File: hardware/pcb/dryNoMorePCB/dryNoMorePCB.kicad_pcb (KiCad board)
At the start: 2 copper layers, 76.2 x 48.6 mm, 47 parts, among them J10 Barrel_Jack_MountingPin, J11 Conn_01x03, J12 Conn_01x03, J13 Conn_01x02, J14 ETH_W5500, J15 Conn_01x02, J16 Conn_01x02, J17 Conn_01x02, J18 GND, J19 GND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

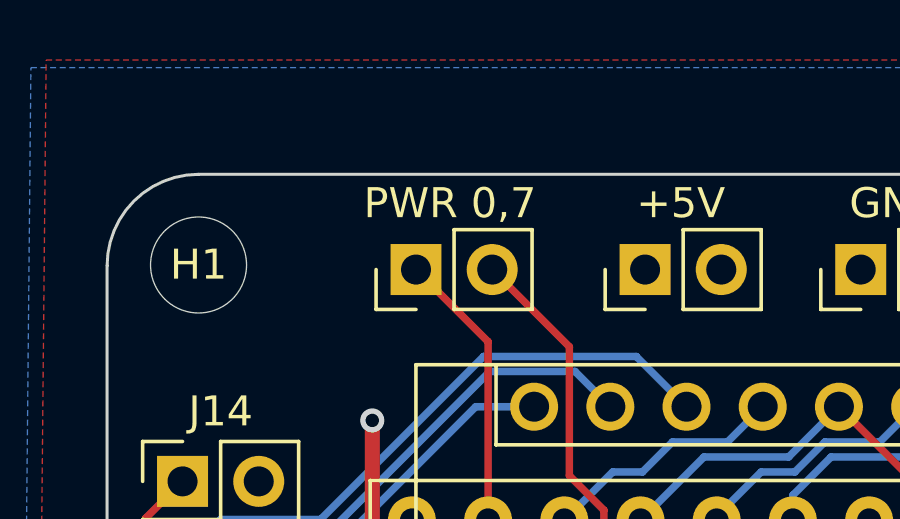
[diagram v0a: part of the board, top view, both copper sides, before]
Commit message: pcb: update pwr label
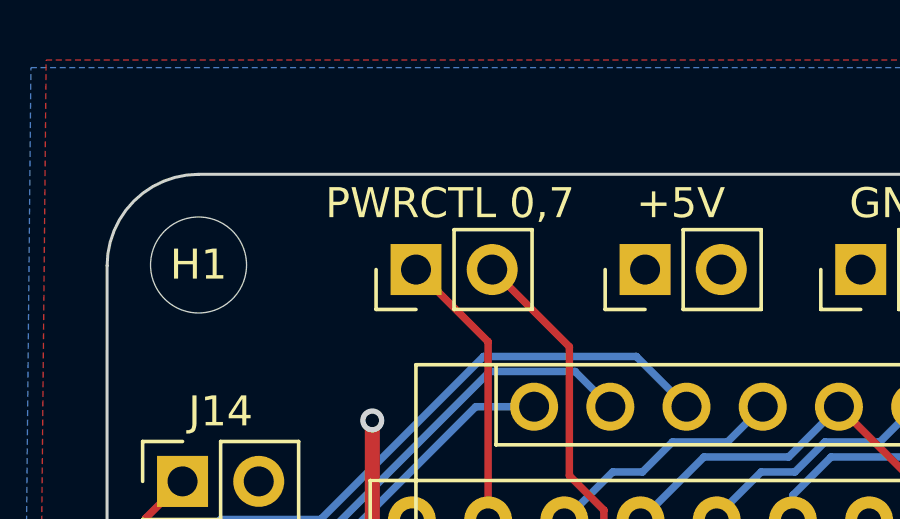
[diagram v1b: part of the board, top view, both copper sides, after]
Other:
- board text added: "PWRCTL 0,7"
- board text removed: "PWR 0,7"
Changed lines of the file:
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@@
     (effects (font (size 1 1) (thickness 0.15)))
   )
-  (gr_text "PWR 0,7" (at 84.582 79.3242) (layer "F.SilkS")
+  (gr_text "PWRCTL 0,7" (at 84.582 79.3242) (layer "F.SilkS")
     (effects (font (size 1 1) (thickness 0.15)))
   )

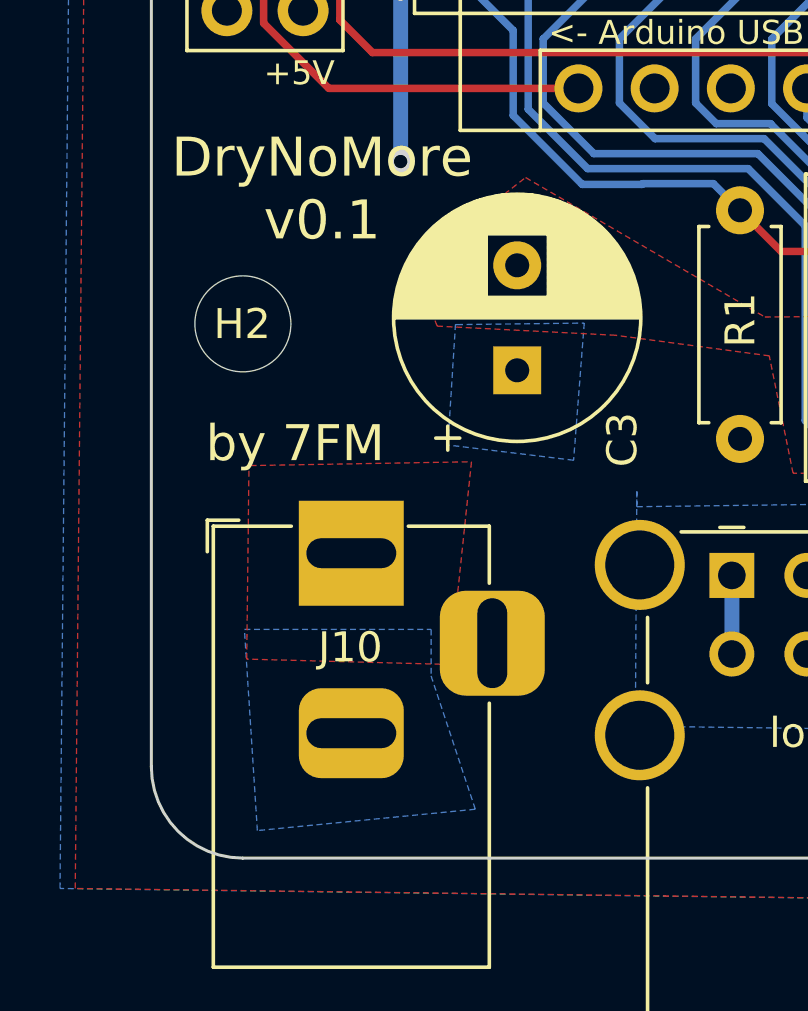
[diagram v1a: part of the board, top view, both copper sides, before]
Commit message: hardware: fix input voltage polarity (J10), pump version
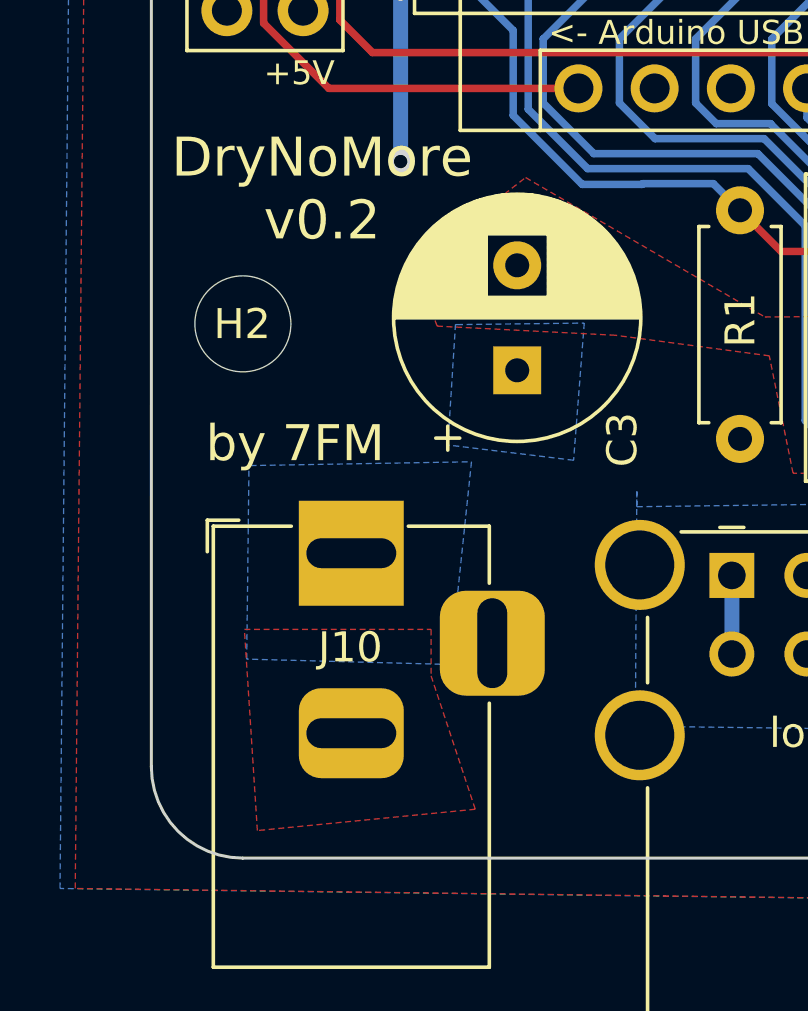
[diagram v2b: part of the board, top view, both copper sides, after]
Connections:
- J10 pad 1: GND -> +5V
- J10 pad 2: +5V -> GND
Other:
- board text added: "DryNoMore v0.2"
- board text removed: "DryNoMore v0.1"
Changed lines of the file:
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@@
     (fp_line (start -0.003213 -4.505425) (end 0.8 -3.75) (layer "F.Fab") (width 0.1))
     (pad "1" thru_hole rect locked (at 0 0 90) (size 3.5 3.5) (drill oval 1 3) (layers *.Cu *.Mask)
-      (net 4 "GND") (pintype "passive"))
-    (pad "2" thru_hole roundrect locked (at -6 0 90) (size 3 3.5) (drill oval 1 3) (layers *.Cu *.Mask) (roundrect_rratio 0.25)
       (net 26 "+5V") (pintype "passive"))
+    (pad "2" thru_hole roundrect locked (at -6 0 90) (size 3 3.5) (drill oval 1 3) (layers *.Cu *.Mask) (roundrect_rratio 0.25)
+      (net 4 "GND") (pintype "passive"))
     (pad "3" thru_hole roundrect locked (at -3 4.7 90) (size 3.5 3.5) (drill oval 3 1) (layers *.Cu *.Mask) (roundrect_rratio 0.25))
     (model "${KICAD6_3DMODEL_DIR}/Connector_BarrelJack.3dshapes/BarrelJack_Horizontal.wrl"
@@
     (effects (font (size 1 1) (thickness 0.15)))
   )
-  (gr_text "DryNoMore\nv0.1" (at 78.8416 104.6988) (layer "F.SilkS")
+  (gr_text "DryNoMore\nv0.2" (at 78.8416 104.6988) (layer "F.SilkS")
     (effects (font (size 1.3 1.3) (thickness 0.2)))
   )
@@
     (connect_pads (clearance 0.508))
     (min_thickness 0.254) (filled_areas_thickness no)
-    (fill yes (thermal_gap 0.508) (thermal_bridge_width 2))
+    (fill yes (thermal_gap 0.508) (thermal_bridge_width 0.508))
     (polygon
       (pts
-        (xy 83.1088 120.5484)
-        (xy 76.327 120.3706)
-        (xy 76.4032 113.9698)
-        (xy 76.454 113.919)
-        (xy 83.82 113.792)
+        (xy 150.876 129.032)
+        (xy 70.612 128.016)
+        (xy 71.12 74.549)
+        (xy 150.876 74.549)
       )
     )
@@
     (connect_pads (clearance 0.508))
     (min_thickness 0.254) (filled_areas_thickness no)
-    (fill yes (thermal_gap 0.508) (thermal_bridge_width 0.508))
+    (fill yes (thermal_gap 0.508) (thermal_bridge_width 2))
     (polygon
       (pts
-        (xy 150.876 129.032)
-        (xy 70.612 128.016)
-        (xy 71.12 74.549)
-        (xy 150.876 74.549)
+        (xy 82.4738 120.9294)
+        (xy 83.947 125.3744)
+        (xy 76.6826 126.0856)
+        (xy 76.2508 119.38)
+        (xy 82.4738 119.38)
       )
     )
@@
     (connect_pads (clearance 0.508))
     (min_thickness 0.254) (filled_areas_thickness no)
-    (fill yes (thermal_gap 0.508) (thermal_bridge_width 0.508))
+    (fill yes (thermal_gap 0.508) (thermal_bridge_width 2))
     (polygon
       (pts
-        (xy 151.384 82.296)
-        (xy 150.876 129.032)
-        (xy 70.104 128.016)
-        (xy 70.612 74.803)
-        (xy 151.384 74.803)
+        (xy 83.1088 120.5484)
+        (xy 76.327 120.3706)
+        (xy 76.4032 113.9698)
+        (xy 76.454 113.919)
+        (xy 83.82 113.792)
       )
     )
@@
     (connect_pads (clearance 0.508))
     (min_thickness 0.254) (filled_areas_thickness no)
-    (fill yes (thermal_gap 0.508) (thermal_bridge_width 2))
+    (fill yes (thermal_gap 0.508) (thermal_bridge_width 0.508))
     (polygon
       (pts
-        (xy 82.4738 120.9294)
-        (xy 83.947 125.3744)
-        (xy 76.6826 126.0856)
-        (xy 76.2508 119.38)
-        (xy 82.4738 119.38)
+        (xy 151.384 82.296)
+        (xy 150.876 129.032)
+        (xy 70.104 128.016)
+        (xy 70.612 74.803)
+        (xy 151.384 74.803)
       )
     )

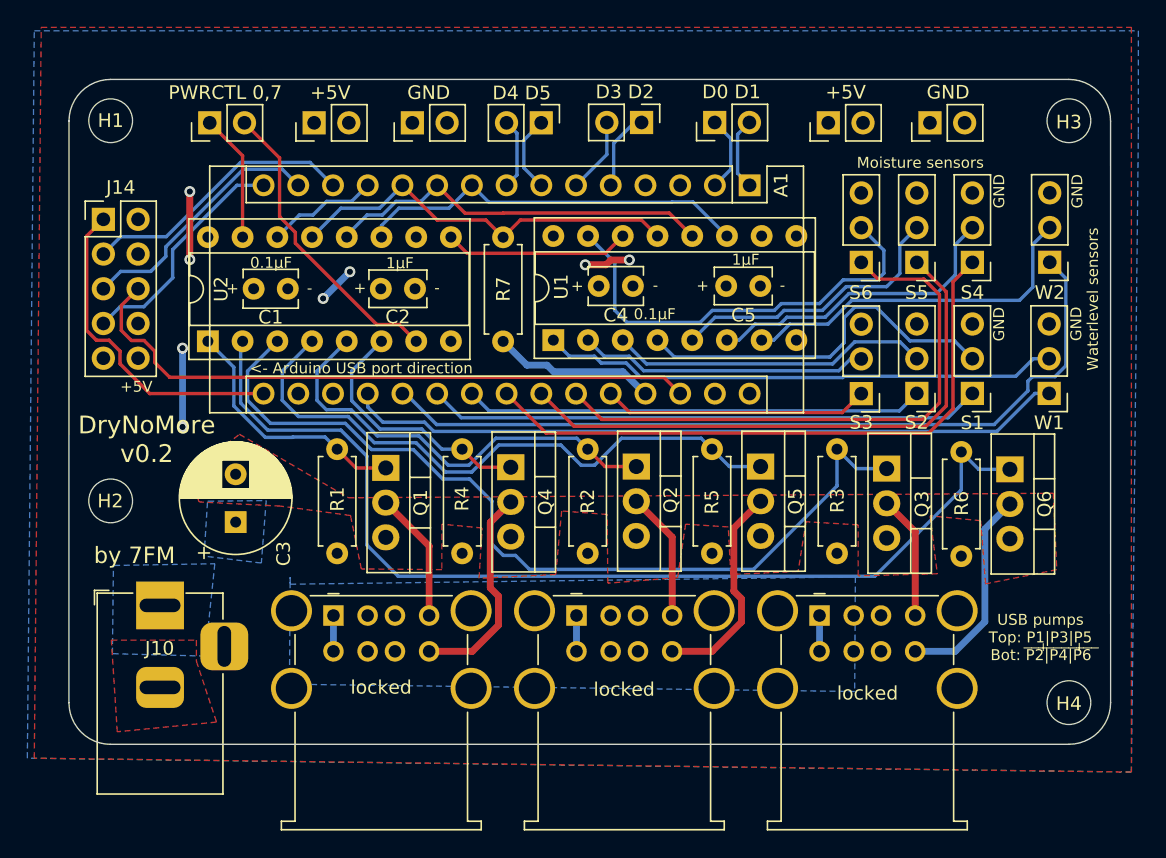
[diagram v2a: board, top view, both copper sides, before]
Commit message: new hardware revision: add mosfet to switch off the ethernet module
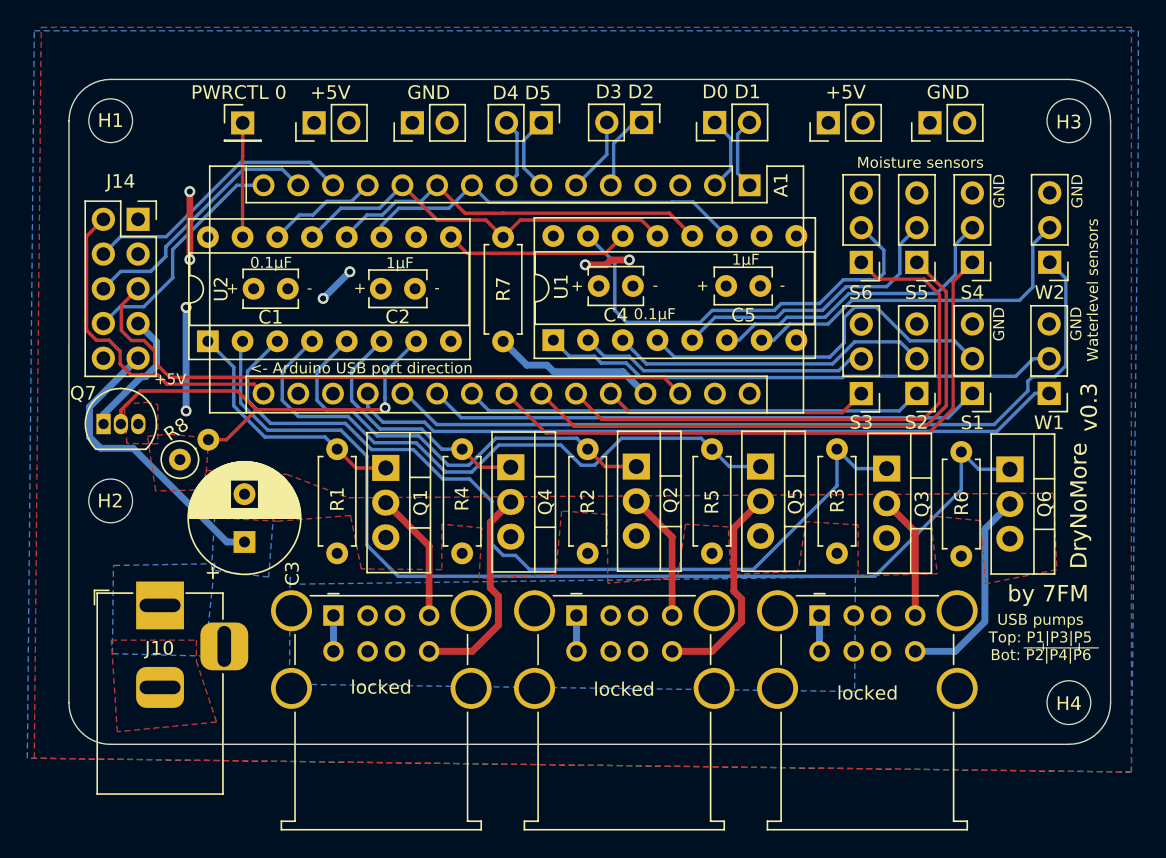
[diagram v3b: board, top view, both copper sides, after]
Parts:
- added Q7: Q_NMOS_DGS, Package_TO_SOT_THT:TO-92_Inline, F.Cu at (75.7, 103.6)
- added R8: 10k, Resistor_THT:R_Axial_DIN0207_L6.3mm_D2.5mm_P2.54mm_Vertical, F.Cu at (81.3, 106.2)
- J13: value Conn_01x02 -> Conn_01x01; footprint Connector_PinHeader_2.54mm:PinHeader_1x02_P2.54mm_Vertical -> Connector_PinHeader_2.54mm:PinHeader_1x01_P2.54mm_Vertical
- J14: footprint Connector_PinHeader_2.54mm:PinHeader_2x05_P2.54mm_Vertical -> Connector_PinSocket_2.54mm:PinSocket_2x05_P2.54mm_Vertical
- moved J14 2.54 mm to (78.2, 88.6)
- moved J13 2.41 mm to (85.9, 81.5), turned to 0 degrees
- moved C3 1.59 mm to (86.0, 112.2)
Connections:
- J14 pad 1: /ETH_SCLK -> unconnected-(J14-Pad1)
- J14 pad 10: +5V -> unconnected-(J14-Pad10)
- J14 pad 2: unconnected-(J14-Pad2) -> /ETH_SCLK
- J14 pad 3: /ETH_CS -> /ETH_INT
- J14 pad 4: /ETH_INT -> /ETH_CS
- J14 pad 5: /ETH_MOSI -> /ETH_RST
- J14 pad 6: /ETH_RST -> /ETH_MOSI
- J14 pad 7: /ETH_MISO -> /ETH_PWR
- J14 pad 8: GND -> /ETH_MISO
- J14 pad 9: unconnected-(J14-Pad9) -> +5V
- U2 pad 7: /UNUSED_PWR_CTRL_2 -> /ETH_CTRL
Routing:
- net /ETH_CTRL: track 0.00 -> 31.8 mm, vias 0 -> 1
- net /UNUSED_PWR_CTRL_2: track 22.2 -> 0.00 mm
- net +5V: track 28.1 -> 49.8 mm
- net /ETH_PWR: track 0.00 -> 9.71 mm
- net GND: track 8.53 -> 10.3 mm
- net /UNUSED_PWR_CTRL_1: track 9.36 -> 8.36 mm
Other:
- board text added: "DryNoMore"
- board text added: "PWRCTL 0"
- board text added: "v0.3"
- board text removed: "DryNoMore v0.2"
- board text removed: "PWRCTL 0,7"

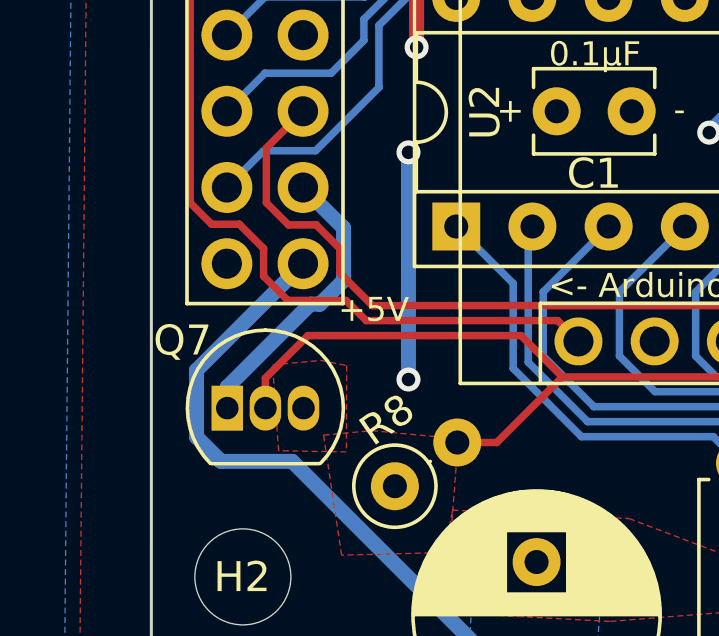
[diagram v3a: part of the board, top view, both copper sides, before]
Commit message: change nmos from DGS to SGD pinout to match an 2N7000
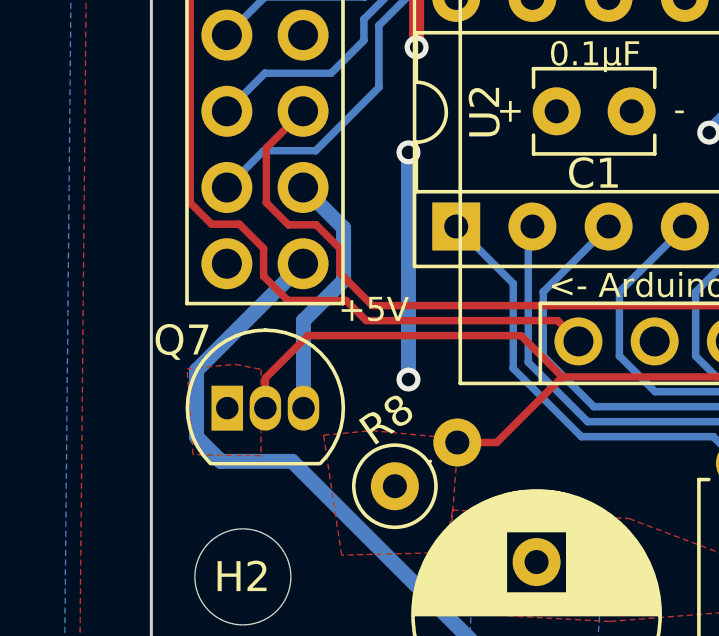
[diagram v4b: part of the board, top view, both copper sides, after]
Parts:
- Q7: value Q_NMOS_DGS -> Q_NMOS_SGD
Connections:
- Q7 pad 1: /ETH_PWR -> GND
- Q7 pad 3: GND -> /ETH_PWR
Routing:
- net /ETH_PWR: track 9.71 -> 8.47 mm
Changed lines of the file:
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@@
       (effects (font (size 1 1) (thickness 0.15)))
     )
-    (fp_text value "Q_NMOS_DGS" (at 1.27 2.79) (layer "F.Fab")
+    (fp_text value "Q_NMOS_SGD" (at 1.27 2.79) (layer "F.Fab")
       (effects (font (size 1 1) (thickness 0.15)))
     )
@@
     (fp_arc (start 1.27 -2.48) (mid 3.561221 -0.949055) (end 3.023625 1.753625) (layer "F.Fab") (width 0.1))
     (pad "1" thru_hole rect (at 0 0) (size 1.05 1.5) (drill 0.75) (layers *.Cu *.Mask)
-      (net 65 "/ETH_PWR") (pinfunction "D") (pintype "passive"))
+      (net 4 "GND") (pinfunction "S") (pintype "passive"))
     (pad "2" thru_hole oval (at 1.27 0) (size 1.05 1.5) (drill 0.75) (layers *.Cu *.Mask)
       (net 67 "/ETH_CTRL") (pinfunction "G") (pintype "input"))
     (pad "3" thru_hole oval (at 2.54 0) (size 1.05 1.5) (drill 0.75) (layers *.Cu *.Mask)
-      (net 4 "GND") (pinfunction "S") (pintype "passive"))
+      (net 65 "/ETH_PWR") (pinfunction "D") (pintype "passive"))
     (model "${KICAD6_3DMODEL_DIR}/Package_TO_SOT_THT.3dshapes/TO-92_Inline.wrl"
       (offset (xyz 0 0 0))
@@
   (segment (start 143.6624 93.5482) (end 143.6624 90.436042) (width 0.25) (layer "B.Cu") (net 64))
   (segment (start 142.6892 94.5214) (end 143.6624 93.5482) (width 0.25) (layer "B.Cu") (net 64))
-  (segment (start 79.5566 97.5652) (end 78.2066 96.2152) (width 0.5) (layer "B.Cu") (net 65))
-  (segment (start 78.444776 100.1052) (end 75.68 102.869976) (width 0.5) (layer "B.Cu") (net 65))
-  (segment (start 79.5566 99.314389) (end 79.5566 97.5652) (width 0.5) (layer "B.Cu") (net 65))
-  (segment (start 78.765789 100.1052) (end 79.5566 99.314389) (width 0.5) (layer "B.Cu") (net 65))
-  (segment (start 78.765789 100.1052) (end 78.444776 100.1052) (width 0.5) (layer "B.Cu") (net 65))
-  (segment (start 75.68 102.869976) (end 75.68 103.57) (width 0.5) (layer "B.Cu") (net 65))
+  (segment (start 79.5566 99.314389) (end 78.22 100.650989) (width 0.5) (layer "B.Cu") (net 65))
+  (segment (start 78.22 100.650989) (end 78.22 103.57) (width 0.5) (layer "B.Cu") (net 65))
+  (segment (start 79.5566 97.5652) (end 79.5566 99.314389) (width 0.5) (layer "B.Cu") (net 65))
+  (segment (start 78.2066 96.2152) (end 79.5566 97.5652) (width 0.5) (layer "B.Cu") (net 65))
   (segment (start 76.95 102.57) (end 76.95 103.57) (width 0.25) (layer "F.Cu") (net 67))
   (segment (start 96.28 102.39) (end 96.14 102.53) (width 0.25) (layer "F.Cu") (net 67))
@@
     (polygon
       (pts
-        (xy 79.66 102.15)
-        (xy 79.65 105.03)
-        (xy 77.39 104.99)
-        (xy 77.19 102.13)
-        (xy 78.8 101.98)
+        (xy 76.81 102.28)
+        (xy 76.8 105.16)
+        (xy 74.54 105.12)
+        (xy 74.34 102.26)
+        (xy 75.95 102.11)
       )
     )
